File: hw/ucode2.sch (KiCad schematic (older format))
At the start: 14 parts, among them U801 74HC00, U802 74HC590, U803 27C64, U804 27C64, U805 27C64, U806 27C64, U807 74HCT175, U808 74HCT175, U809 74HCT175, U810 74HCT175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

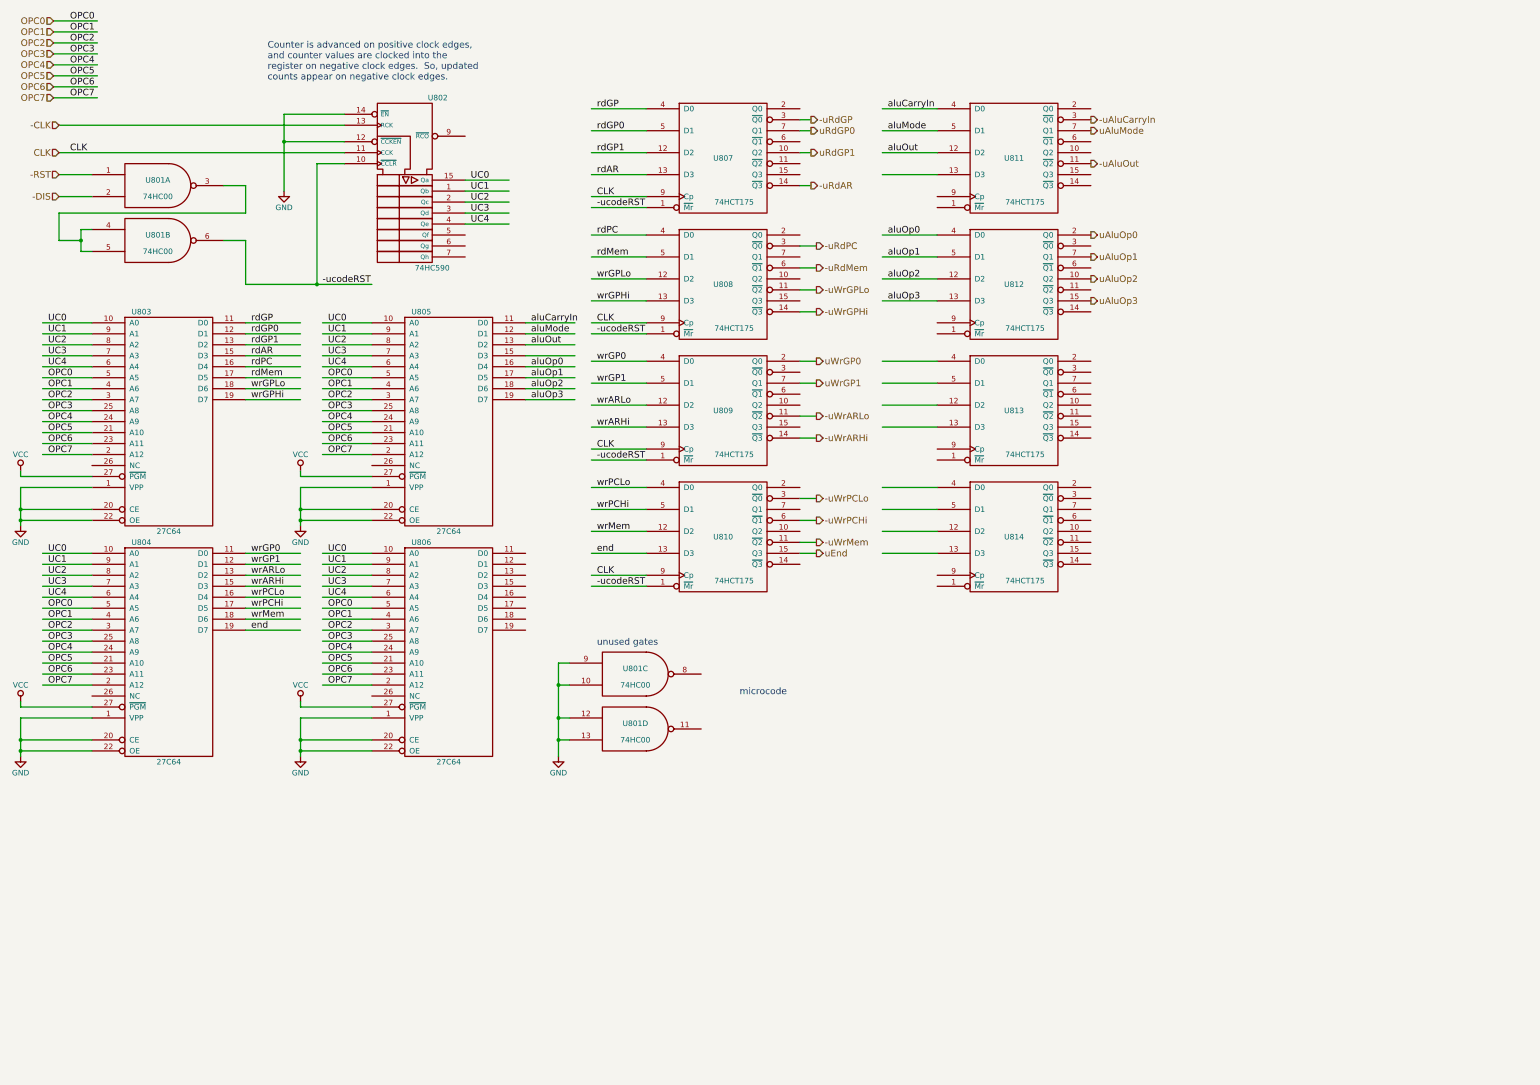
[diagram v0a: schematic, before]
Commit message: implemented conditional branch logic
This requires us to put some combinational logic
behind the '175 registers, based on condition code
signals.  Adds three chips.  Also, added microcode
signals to drive the external address bus and to
send an increment pulse to the program counter.

There are only two unused microcode bits at this
point!
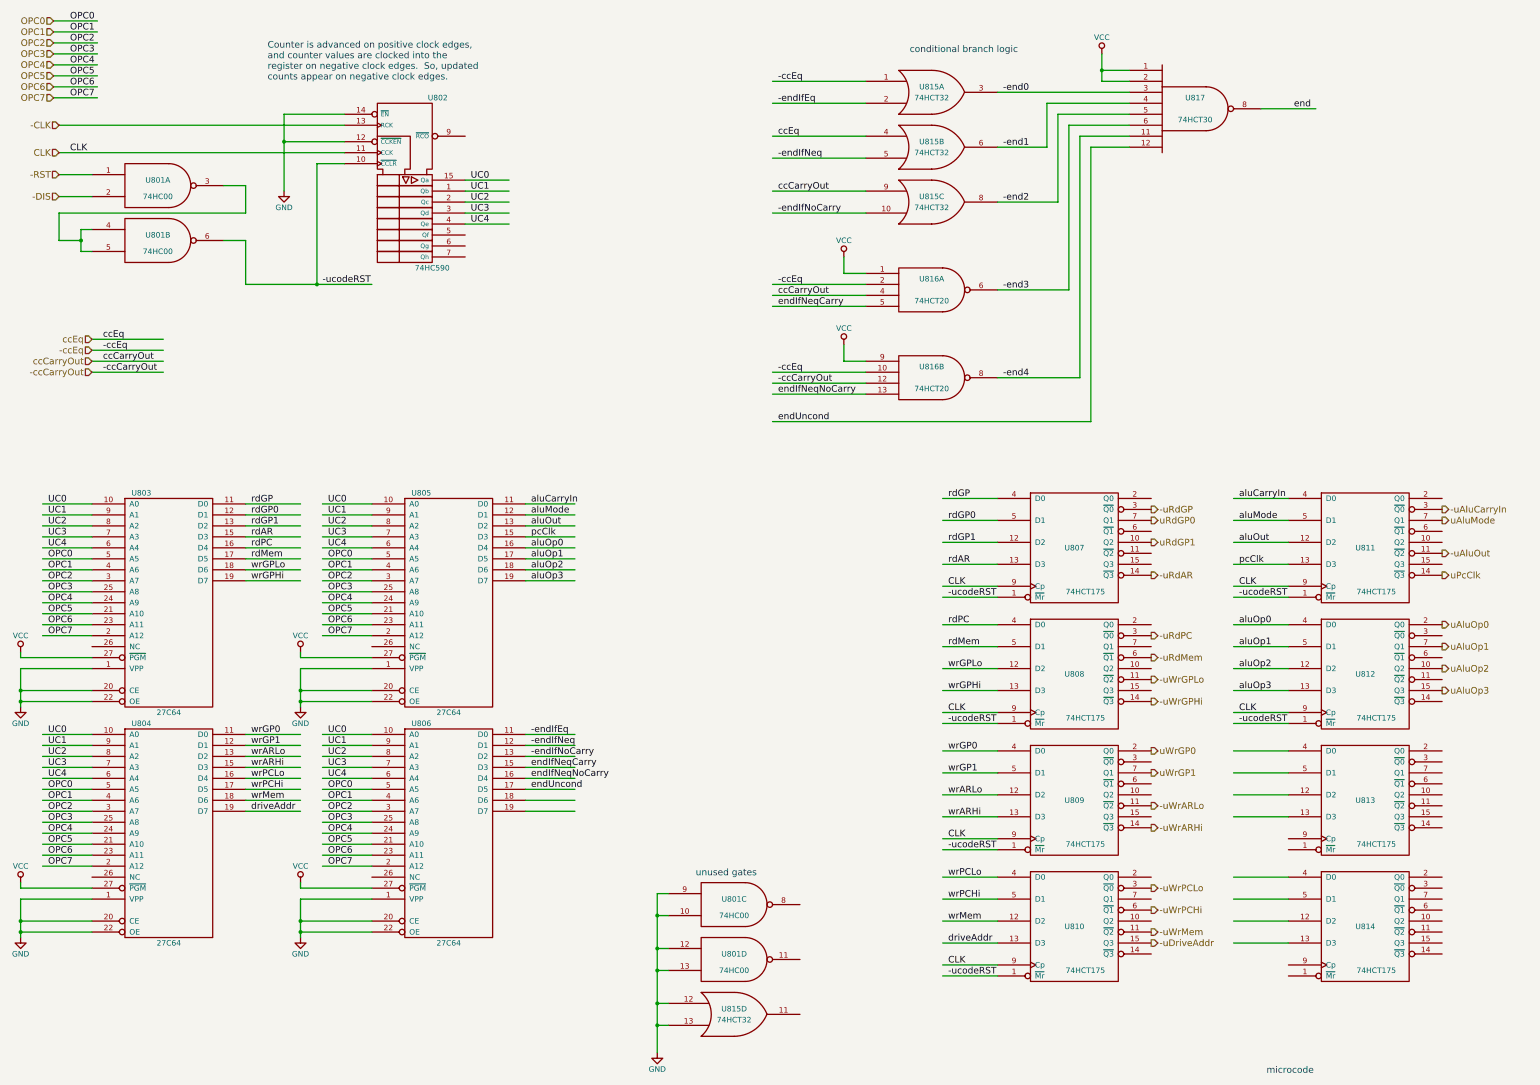
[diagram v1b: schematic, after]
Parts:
- added U815: 74HCT32, symbol 74LS32
- added U816: 74HCT20, symbol 74LS20
- added U817: 74HCT30, symbol 74LS30
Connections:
- net labels added: -ccCarryOut, -ccEq, -end0, -end1, -end2, -end3, -end4, -endIfEq, -endIfNeq, -endIfNoCarry, -uDriveAddr, ccCarryOut, ccEq, driveAddr, endIfNeqCarry, endIfNeqNoCarry, endUncond, pcClk, uPcClk
- net labels removed: uEnd
- wire segments 194 -> 248
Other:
- note added: "conditional branch logic"
- moved on the sheet: U801C, U801D, U803, U804, U805, U806, U807, U808, U809, U810, U811, U812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

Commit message: added uEnd output, use custom sheet size
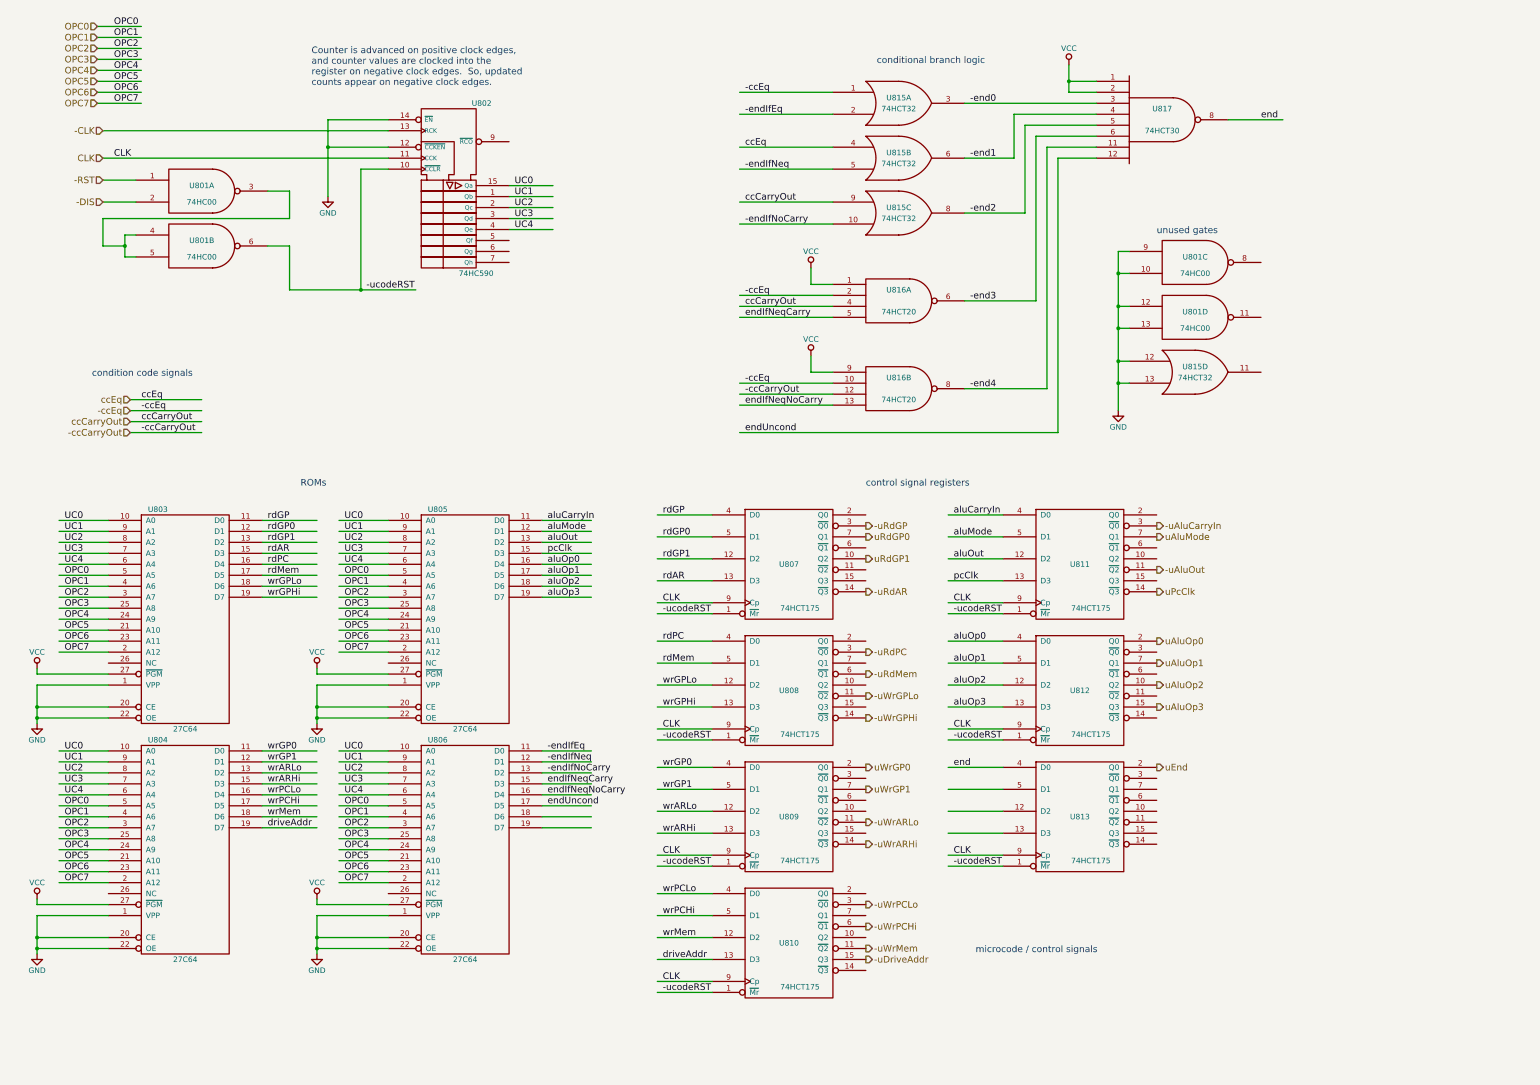
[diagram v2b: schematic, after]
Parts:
- removed U814: 74HCT175, symbol 74LS175
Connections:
- net labels added: uEnd
- wire segments 248 -> 246
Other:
- note added: "ROMs"
- note added: "condition code signals"
- note added: "control signal registers"
- note added: "microcode / control signals"
- note removed: "microcode"
- moved on the sheet: U801A, U801B, U801C, U801D, U802, U803, U804, U805, U806, U807, U808, U809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

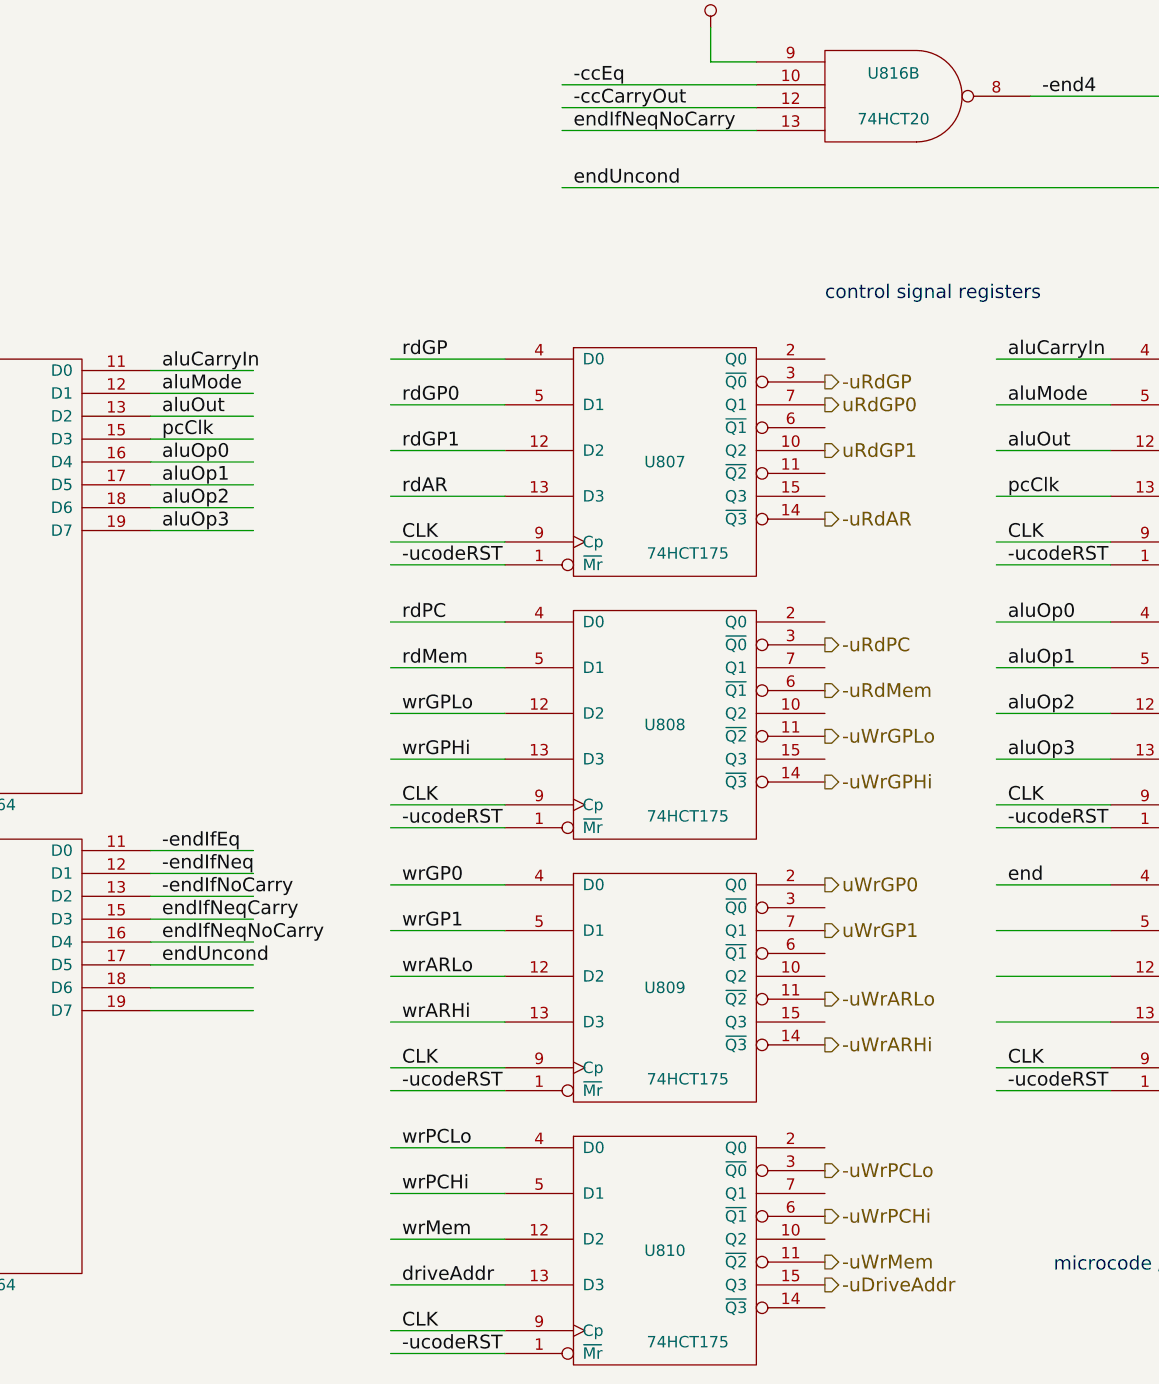
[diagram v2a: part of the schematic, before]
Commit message: -endUncond needs to be active-low
Also, fixed mistaken placement of -uDriveAddr
output.
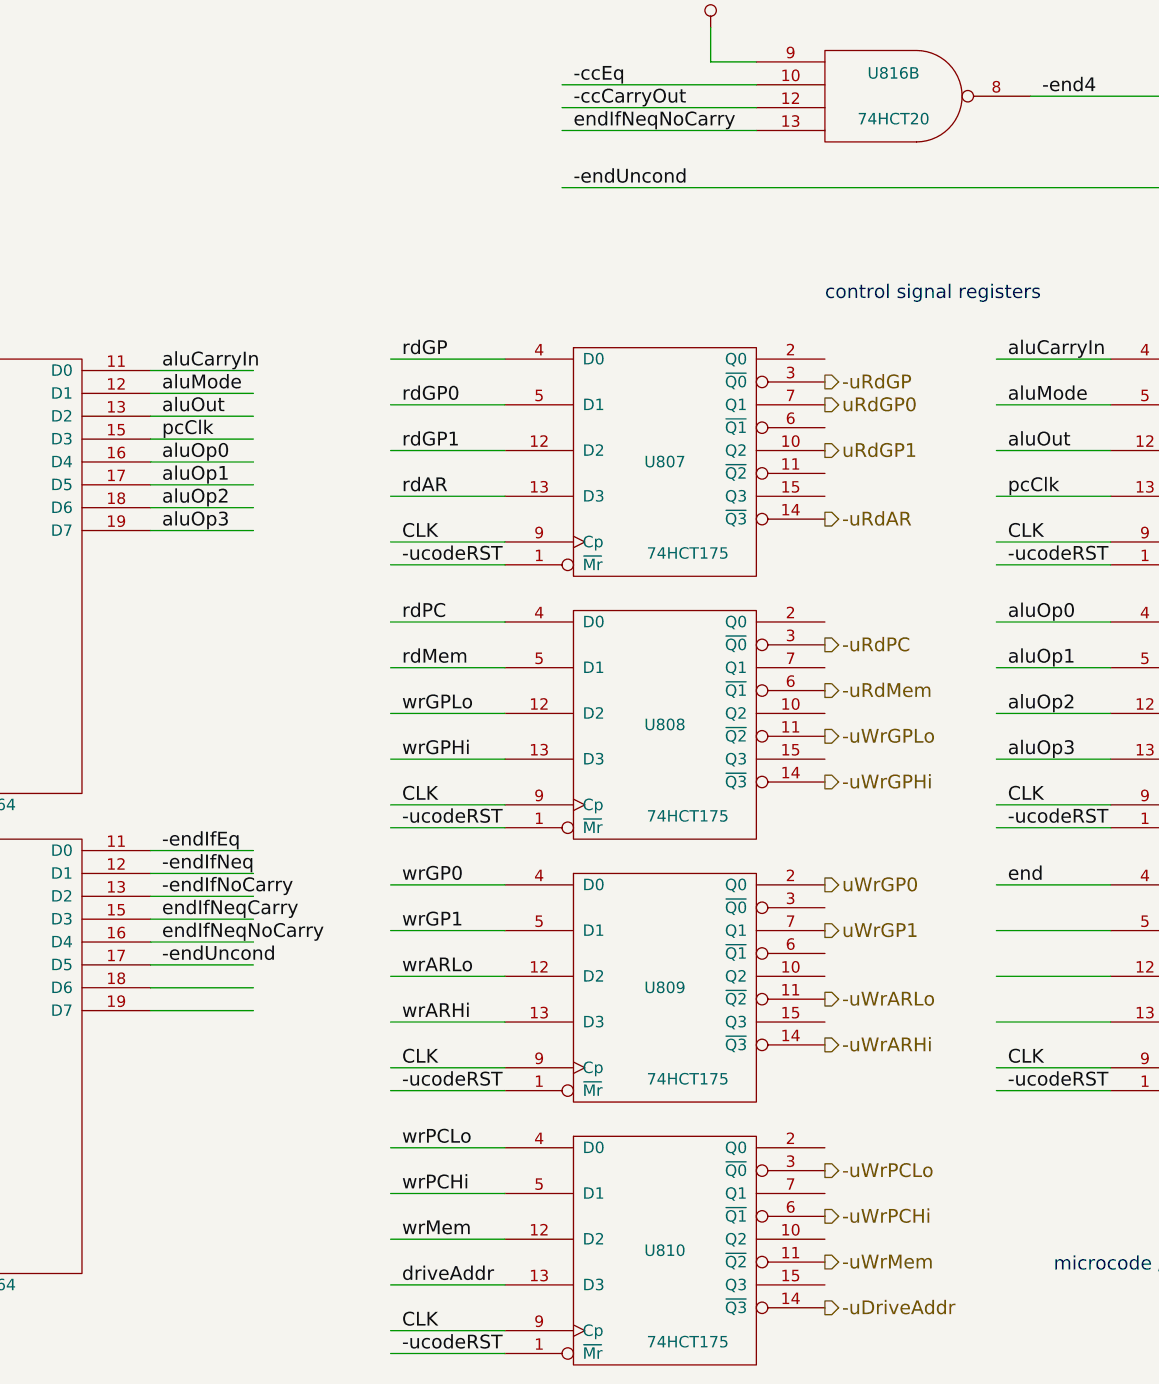
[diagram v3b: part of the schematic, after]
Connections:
- net labels added: -endUncond
- net labels removed: endUncond
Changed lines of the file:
@@
 Text Label 9250 4000 0    60   ~ 0
 -end4
-Text Label 7200 4400 0    60   ~ 0
-endUncond
 Wire Wire Line
 	11600 1550 12100 1550
@@
 Text Label 6450 9200 0    60   ~ 0
 driveAddr
-Text HLabel 8300 9200 2    60   Output ~ 0
+Text HLabel 8300 9300 2    60   Output ~ 0
 -uDriveAddr
 Wire Wire Line
@@
 Text Label 5400 7700 0    60   ~ 0
 endIfNeqNoCarry
-Text Label 5400 7800 0    60   ~ 0
-endUncond
 Text Label 9100 5950 0    60   ~ 0
 CLK
@@
 Text Notes 8300 4900 0    60   ~ 0
 control signal registers
+Text Label 5400 7800 0    60   ~ 0
+-endUncond
+Text Label 7200 4400 0    60   ~ 0
+-endUncond
 $EndSCHEMATC
